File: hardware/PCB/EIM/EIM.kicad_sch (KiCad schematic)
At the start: 46 parts, among them J1 Conn_02x04, U1 AD9834BRUZ, U2 AD8130ARZ, U3 AD8014ARZ, Y1 OSC 75MHz

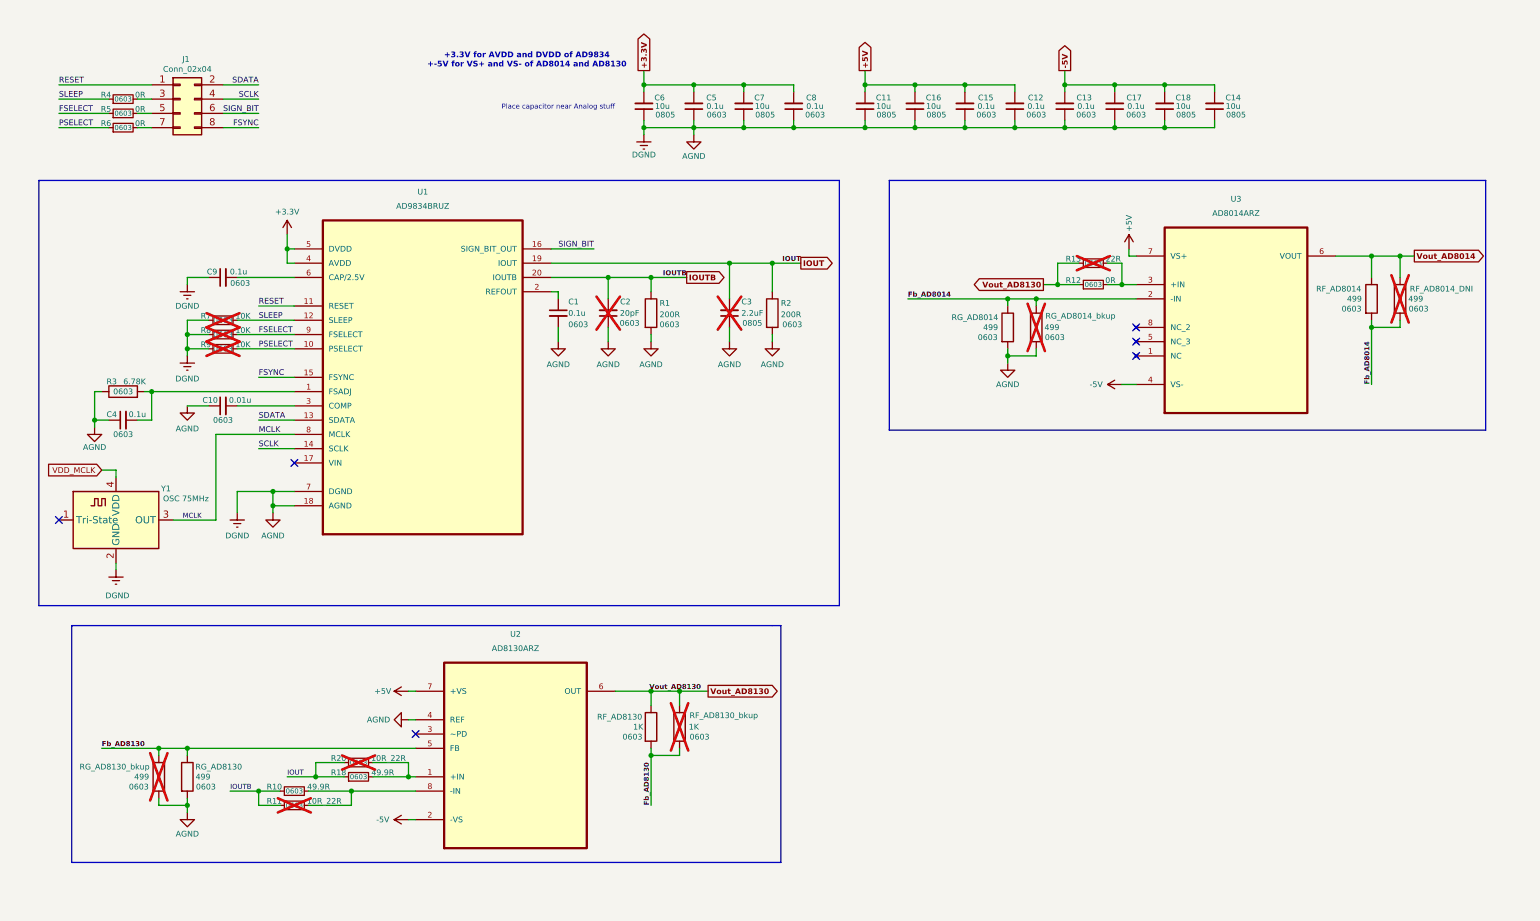
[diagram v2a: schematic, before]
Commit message: MAMS-33 updated schematic for filter block
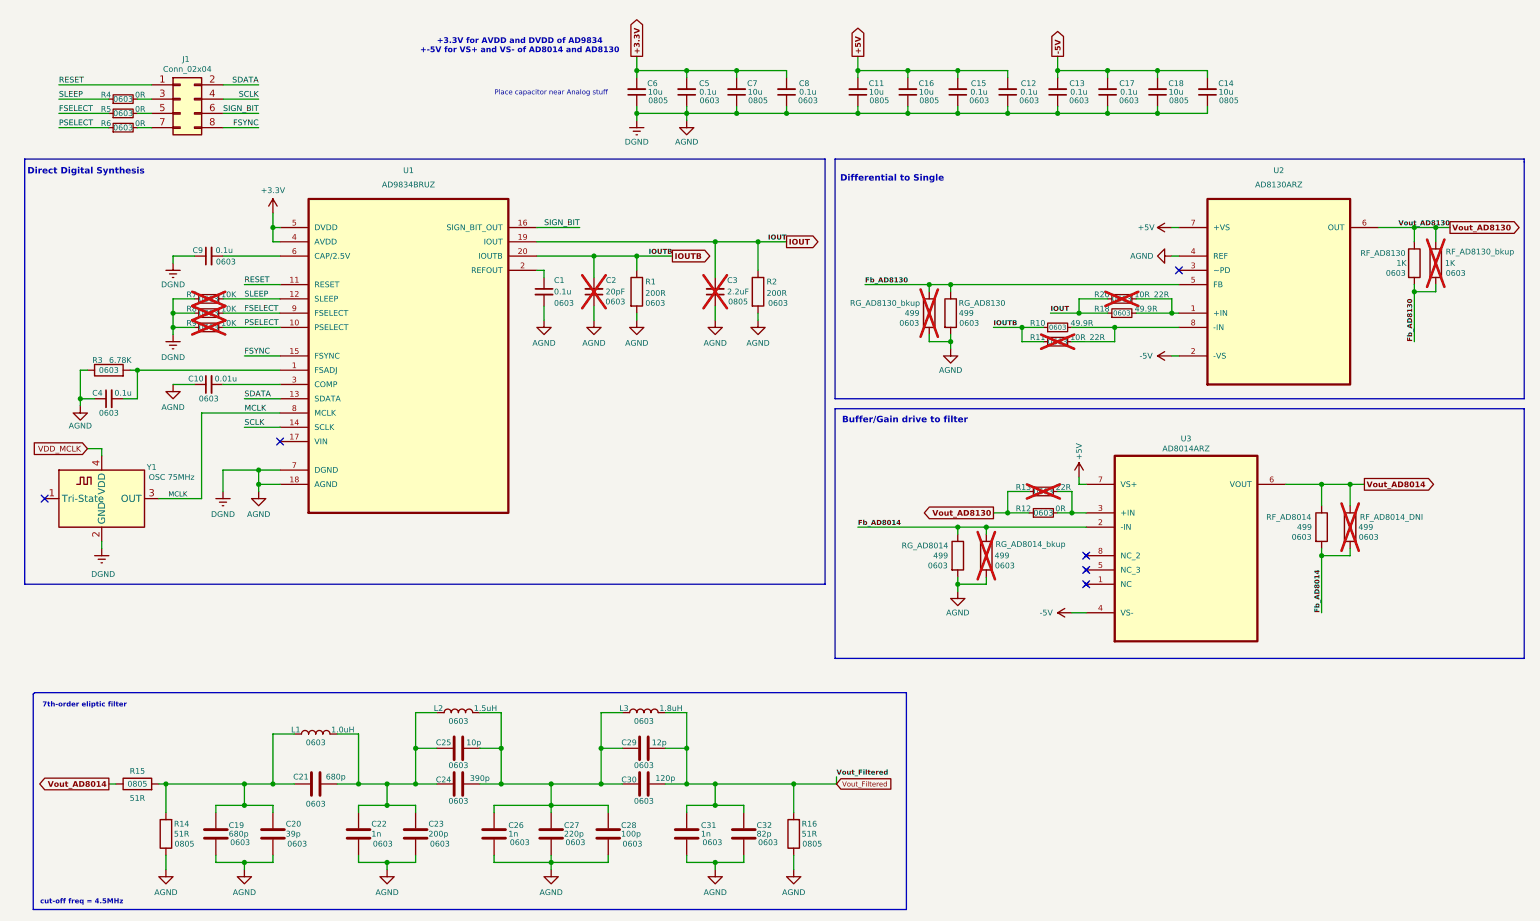
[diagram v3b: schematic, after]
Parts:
- added C19, C21: 680p, 0603, symbol Device:C
- added C20: 39p, 0603, symbol Device:C
- added C22, C26, C31: 1n, 0603, symbol Device:C
- added C23: 200p, 0603, symbol Device:C
- added C24: 390p, 0603, symbol Device:C
- added C25: 10p, 0603, symbol Device:C
- added C27: 220p, 0603, symbol Device:C
- added C28: 100p, 0603, symbol Device:C
- added C29: 12p, 0603, symbol Device:C
- added C30: 120p, 0603, symbol Device:C
- added C32: 82p, 0603, symbol Device:C
- added L1: 1.0uH, 0603, symbol Device:L
- added L2: 1.5uH, 0603, symbol Device:L
- added L3: 1.8uH, 0603, symbol Device:L
- added R14, R15, R16: 51R, 0805, symbol Device:R
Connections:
- net AGND: now also C19.1, C20.1, C22.1, C23.1, C26.1, C27.1, C28.1, C31.1, C32.1, R14.1, R16.1
- net Vout_AD8014: now also R15.1
- new net: C24.1, C25.1, C26.2, C27.2, C28.2, C29.2, C30.2, L2.2, L3.1
- new net: C21.1, C22.2, C23.2, C24.2, C25.2, L1.2, L2.1
- new net: C19.2, C20.2, C21.2, L1.1, R14.2, R15.2
- new net Vout_Filtered: C29.1, C30.1, C31.2, C32.2, L3.2, R16.2
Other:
- note added: "7th-order eliptic filter"
- note added: "Buffer/Gain drive to filter"
- note added: "Differential to Single"
- note added: "Direct Digital Synthesis"
- note added: "cut-off freq = 4.5MHz"
- moved on the sheet: C1, C10, C11, C12, C13, C14, C15, C16, C17, C18, C2, C3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

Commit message: MAMS-33 Fixed footprint lib for DDS, Buffer, Diff-2-Single and Filter block
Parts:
- removed C3: 2.2uF, 0805, symbol Device:C_Small
- removed R10, R18: 49.9R, 0603, symbol Device:R_Small
- removed R11, R20: 10R_22R, 0603, symbol Device:R_Small
- removed R12, R4, R5, R6: 0R, 0603, symbol Device:R_Small
- removed R13: 22R, 0603, symbol Device:R_Small
- removed R16: 51R, 0805, symbol Device:R
- removed R7, R8, R9: 10K, 0603, symbol Device:R_Small
- removed RF_AD8014, RF_AD8014_DNI, RG_AD8014, RG_AD8014_bkup, RG_AD8130, RG_AD8130_bkup: 499, 0603, symbol Device:R
- removed RF_AD8130, RF_AD8130_bkup: 1K, 0603, symbol Device:R
- removed Y1: OSC 75MHz, Oscillator_SMD_2.5x2.0mm, symbol Oscillator:ECS-2520MV-xxx-xx
- added C33: 20p, Capacitor_SMD:C_0603_1608Metric, symbol Device:C_Small
- added R10, R18: 10R_22R, Resistor_SMD:R_0603_1608Metric, symbol Device:R
- added R11, R9: 49.9, Resistor_SMD:R_0603_1608Metric, symbol Device:R
- added R12: 22R, Resistor_SMD:R_0603_1608Metric, symbol Device:R
- added R13, R24, R25, R26, R8: 499, Resistor_SMD:R_0603_1608Metric, symbol Device:R
- added R17, R19, R23, R4: 0R, Resistor_SMD:R_0603_1608Metric, symbol Device:R
- added R20, R22: 1K, Resistor_SMD:R_0603_1608Metric, symbol Device:R
- added R21, R5, R6: 10K, Resistor_SMD:R_0603_1608Metric, symbol Device:R
- added R27: 51R, Resistor_SMD:R_0805_2012Metric, symbol Device:R
- added R7: 6.8K, Resistor_SMD:R_0603_1608Metric, symbol Device:R
- added U4: AD8130ARZ, AD8130ARZ:SOIC127P600X175-8N, symbol AD8130ARZ:AD8130ARZ
- added Y2: 75MHz, Oscillator:Oscillator_SMD_ECS_2520MV-xxx-xx-4Pin_2.5x2.0mm, symbol Oscillator:ECS-2520MV-xxx-xx
- C1, C10, C12, C13, C15, C17, C19, C21, C22, C23, C25, C26, C27, C28, C29, C30, C31, C32, C4, C5, C8, C9: footprint 0603 -> Capacitor_SMD:C_0603_1608Metric; Size (none) -> 0603
- C11, C14, C16, C18, C6, C7: footprint 0805 -> Capacitor_SMD:C_0805_2012Metric; Size (none) -> 0805
- C2: value 20pF -> 20p; footprint 0603 -> Capacitor_SMD:C_0603_1608Metric; Size (none) -> 0603
- C20, C24: footprint 0603 -> Capacitor_SMD:C_0603_1608Metric; SIze (none) -> 0603
- L1, L2, L3: footprint 0603 -> Inductor_SMD:L_0603_1608Metric; Size (none) -> 0603
- R1, R2: footprint 0603 -> Resistor_SMD:R_0603_1608Metric; Size (none) -> 0603
- R14, R15: footprint 0805 -> Resistor_SMD:R_0805_2012Metric; Size (none) -> 0805
- R3: value 6.78K -> 499; footprint 0603 -> Resistor_SMD:R_0603_1608Metric; Size (none) -> 0603
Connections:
- net +5V: now also U4.7 (+VS)
- net -5V: now also U4.2 (-VS)
- net AGND: now also R1.1, R15.1, R2.1, C33.1, R13.1, R21.1, R24.1, R5.1, R6.1, R7.1, R8.1, U4.8 (-IN), Y2.2 (GND); no longer R1.2, R2.2
- net FSELECT: now also R4.1, R6.2
- net Fb_AD8014: now also R13.2, R24.2, R25.1, R26.1
- net Fb_AD8130: now also R3.2, R20.2, R22.2, R8.2
- net IOUT: now also R2.2, C33.2, R11.2, R18.2; no longer R2.1
- net IOUTB: now also R1.2, R10.2, R9.2; no longer R1.1
- net MCLK: now also Y2.3 (OUT)
- net PSELECT: now also R19.1, R21.2
- net SLEEP: now also R17.1, R5.2
- net VDD_MCLK: now also Y2.4 (VDD)
- net Vout_AD8014: now also R25.2, R26.2, R27.1; no longer R15.1
- net Vout_AD8130: now also R12.2, R20.1, R22.1, R23.2
- net Vout_Filtered: now also R15.2, U4.1 (+IN)
- net at U2.8 (-IN): now also R10.1, R9.1
- net at C19.2, C20.2, C21.2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: now also R27.2; no longer R15.2
- net at U2.1 (+IN): now also R11.1, R18.1
- net at C4.2, U1.1 (FSADJ): now also R7.2; no longer R3.2
- net at U3.3 (+IN): now also R12.1, R23.1
- net at J1.7 (Pin_7): now also R19.2
- net at J1.5 (Pin_5): now also R4.2
- net at J1.3 (Pin_3): now also R17.2
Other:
- company: University of Science -> DPEE Lab
- moved on the sheet: C1, C10, C19, C2, C20, C21, C22, C23, C24, C25, C26, C27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

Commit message: MAMS-33: Update schematic for load block and library
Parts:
- added C3, C35, C37, C40, C42, C45, C46, C49, C50, C53: 10u, Capacitor_SMD:C_0805_2012Metric, symbol Device:C_Small
- added C34, C36, C38, C39, C41, C43, C47, C48, C51, C52: 0.1u, Capacitor_SMD:C_0603_1608Metric, symbol Device:C_Small
- added C44: 0.047u, Capacitor_SMD:C_0805_2012Metric, symbol Device:C_Small
- added C54, C55: 1p, Capacitor_SMD:C_0603_1608Metric, symbol Device:C_Small
- added J2, J3, J4, J5: CONSMA002-G, SMA-CONSMA002-G:LINX_CONSMA002-G, symbol SMA:CONSMA002-G
- added R16, R28, R29, R31, R33: 10K, Resistor_SMD:R_0603_1608Metric, symbol Device:R
- added R30: 47R, Resistor_SMD:R_0603_1608Metric, symbol Device:R
- added R32: 100R, Resistor_SMD:R_0603_1608Metric, symbol Device:R
- added U5, U7: AD8066ARZ-R7, AD8066ARZ-R7:SOIC127P600X175-8N, symbol AD8066:AD8066ARZ-R7
- added U6, U8: AD8130ARZ, AD8130ARZ:SOIC127P600X175-8N, symbol AD8130ARZ:AD8130ARZ
- added U9: AD8302ARUZ, AD8302ARUZ:SOP65P640X120-14N, symbol AD8302ARUZ:AD8302ARUZ
- R12: now fitted
- R23: now not fitted
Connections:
- net +5V: now also C3.2, C34.2, C35.2, C36.2, C37.2, C38.2, C46.2, C47.2, C50.2, C51.2, R16.1, R28.1, R31.1, R33.1, U5.8, U6.7 (+VS), U7.8, U8.7 (+VS)
- net -5V: now also C39.2, C40.2, C41.2, C42.2, C43.2, C45.2, C48.2, C49.2, C52.2, C53.2, U5.4, U6.2 (-VS), U7.4, U8.2 (-VS)
- net AGND: now also C3.1, C34.1, C35.1, C36.1, C37.1, C38.1, C39.1, C40.1, C41.1, C42.1, C43.1, C45.1, C46.1, C47.1, C48.1, C49.1, C50.1, C51.1, C52.1, C53.1, J2.S1, J2.S2, J2.S3, J2.S4, J3.S1, J3.S2, J3.S3, J3.S4, J4.S1, J4.S2, J4.S3, J4.S4, J5.S1, J5.S2, J5.S3, J5.S4, R32.2, U6.4 (REF), U6.8 (-IN), U8.4 (REF)
- net at U2.3 (~PD): now also R16.2
- net at U4.3 (~PD): now also R28.2
- net Vout_node_Risolation_AD8065: now reaches U4.4 (REF)
- net Vout_node_Risolation_AD8065: now also C44.1, R30.1, U7.2
- net Vout_node_VCCS_AD8130: now reaches U4.5 (FB)
- net Vout_node_VCCS_AD8130: now also U4.6 (OUT), R29.1
- net Vout_AD8014 renamed Vout_buff
- net Vout_AD8130 renamed Vout_Diff2Sin
- new net: R30.2, U7.1
- new net: C54.1, U5.1
- new net: R33.2, U8.3 (~PD)
- new net: R31.2, U6.3 (~PD)
- new net: C55.2, U5.7
- new net COMM: U9.1 (COMM), U9.7 (COMM)
- new net I+ measurement: J4.1, U5.3
- new net I- measurement: J5.1, U5.6
- new net Over_Current_Protect: U6.6 (OUT)
- new net Vout_R_Curr_Sense: J3.1, R32.1, U6.1 (+IN)
- new net Vout_VCCS: C44.2, J2.1
- new net Vout_node_Rsense: R29.2, U7.3
- new net to_IN+_AD8130: C54.2, U5.2, U8.1 (+IN)
- new net to_IN-_AD8130: C55.1, U5.5, U8.8 (-IN)
- no-connect marks 6 -> 9
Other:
- note added: "LOAD"
- note added: "R29 - Rsense R30 - Risolation C44 - Coupling"
- note added: "Tetrapolar electrodes"
- note added: "Voltage Controlled Current Source"
- note removed: "Place capacitor near Analog stuff"
- moved on the sheet: C1, C10, C11, C12, C13, C14, C15, C16, C17, C18, C19, C2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
